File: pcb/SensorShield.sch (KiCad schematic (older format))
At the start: 58 parts, among them U14 ICE40UP5K-SG48ITR, U15 GD25Q32CTIGR-Memory_Flash

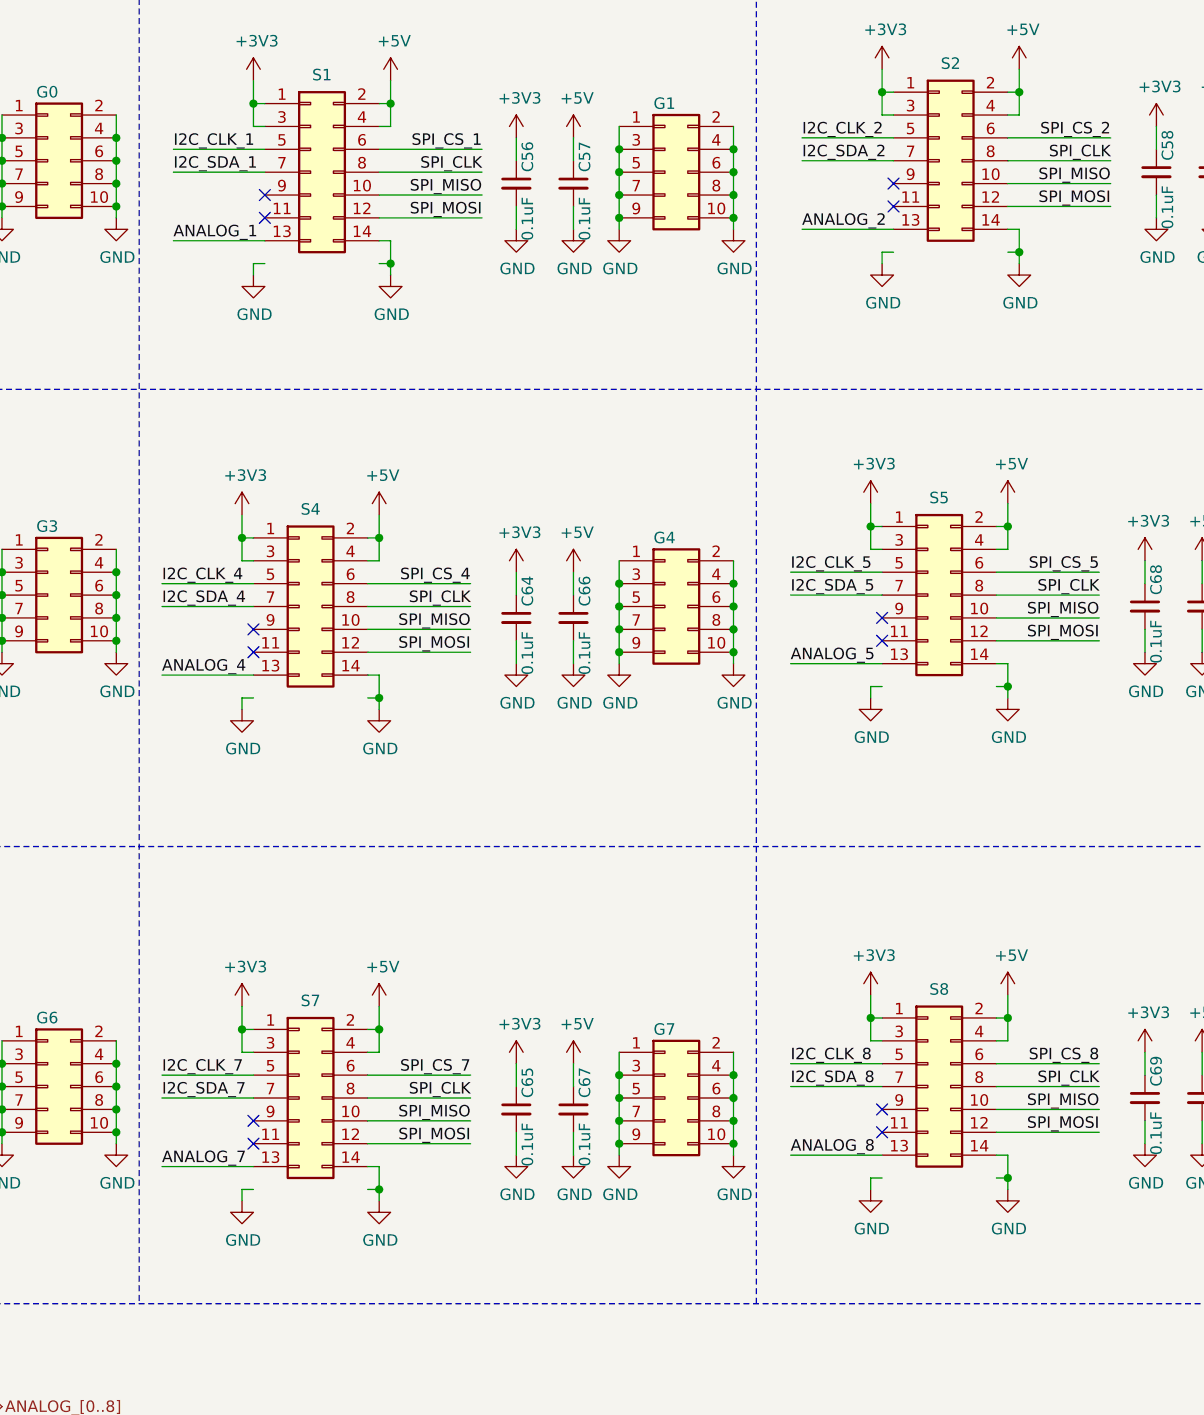
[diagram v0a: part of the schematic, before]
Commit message: routing i2c signals
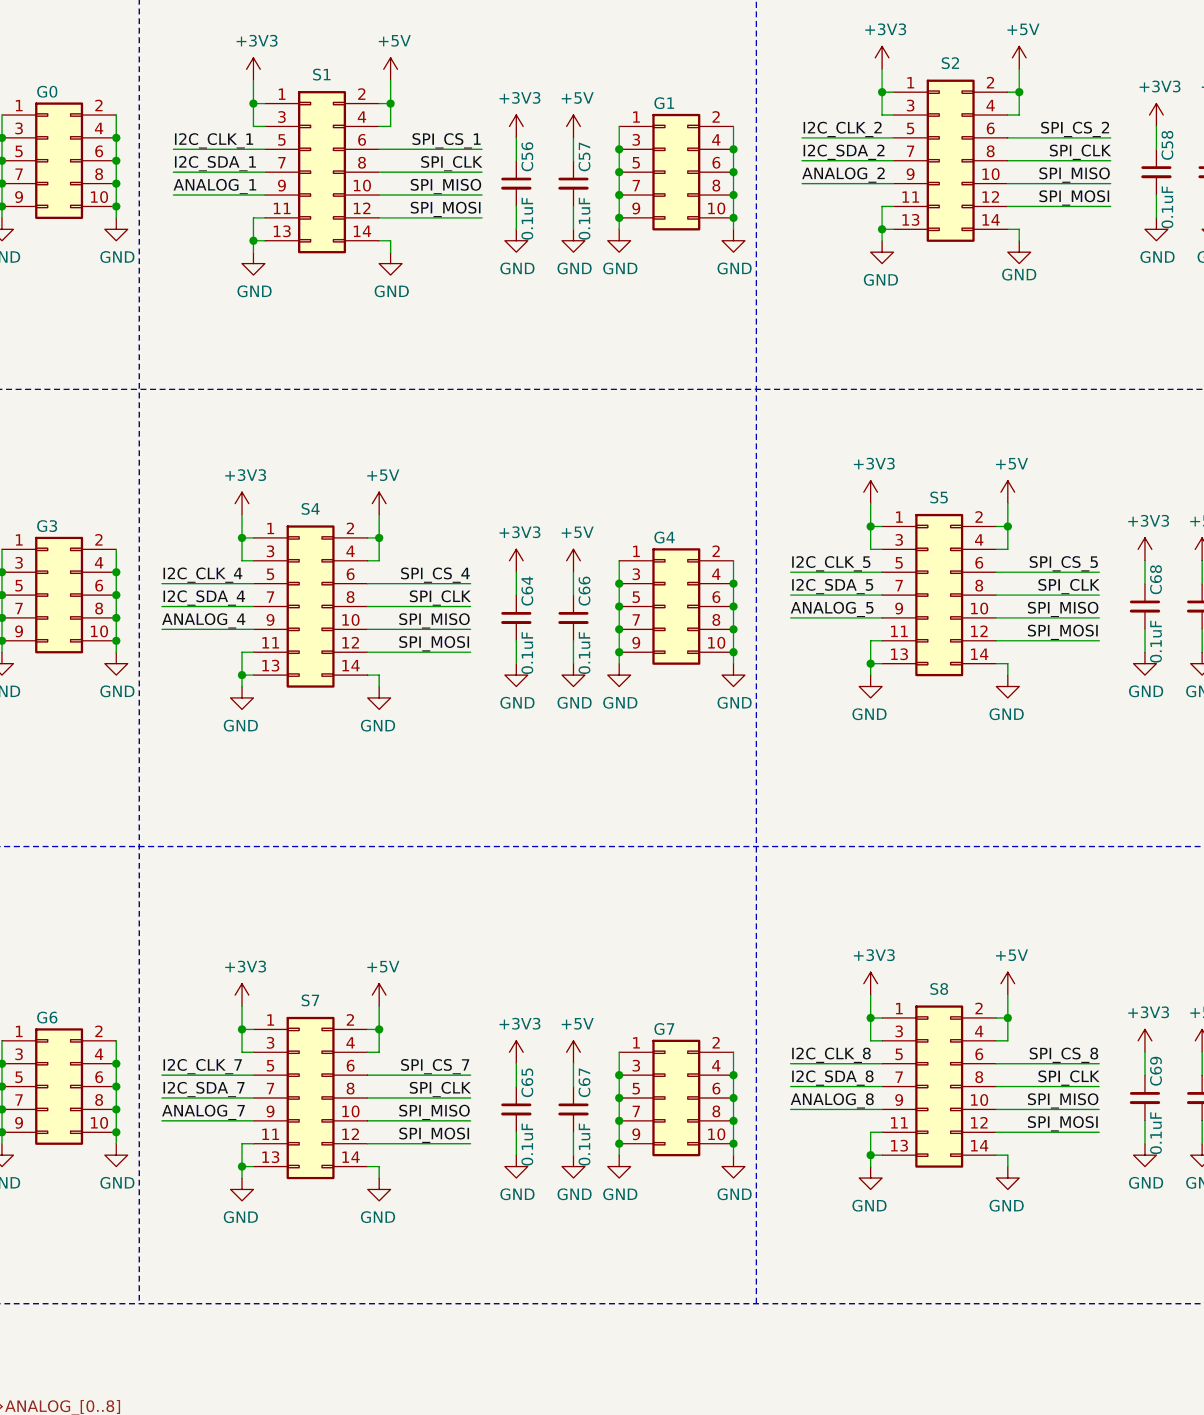
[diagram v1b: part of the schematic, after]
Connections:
- no-connect marks 12 -> 0

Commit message: 2.5V  diode placement
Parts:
- D4: value 1N4148WT-7 -> CDBU0520; symbol UPduino_v3.0:Diode_1N4148W -> Device:D
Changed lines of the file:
@@
 +1.2V_CORE
 $Comp
-L UPduino_v3.0:Diode_1N4148W D?
+L Device:D D?
 U 1 1 5E9D8B98
 P 2450 6300
@@
 AR Path="/5E9C016D/5E9D8B98" Ref="D4"  Part="1"
 F 0 "D4" H 2450 6517 50  0000 C CNN
-F 1 "1N4148WT-7" H 2450 6426 50  0000 C CNN
+F 1 "CDBU0520" H 2450 6426 50  0000 C CNN
 F 2 "Diode_SMD:D_SOD-523" H 2450 6125 50  0001 C CNN
 F 3 "https://www.vishay.com/docs/85748/1n4148w.pdf" H 2450 6300 50  0001 C CNN

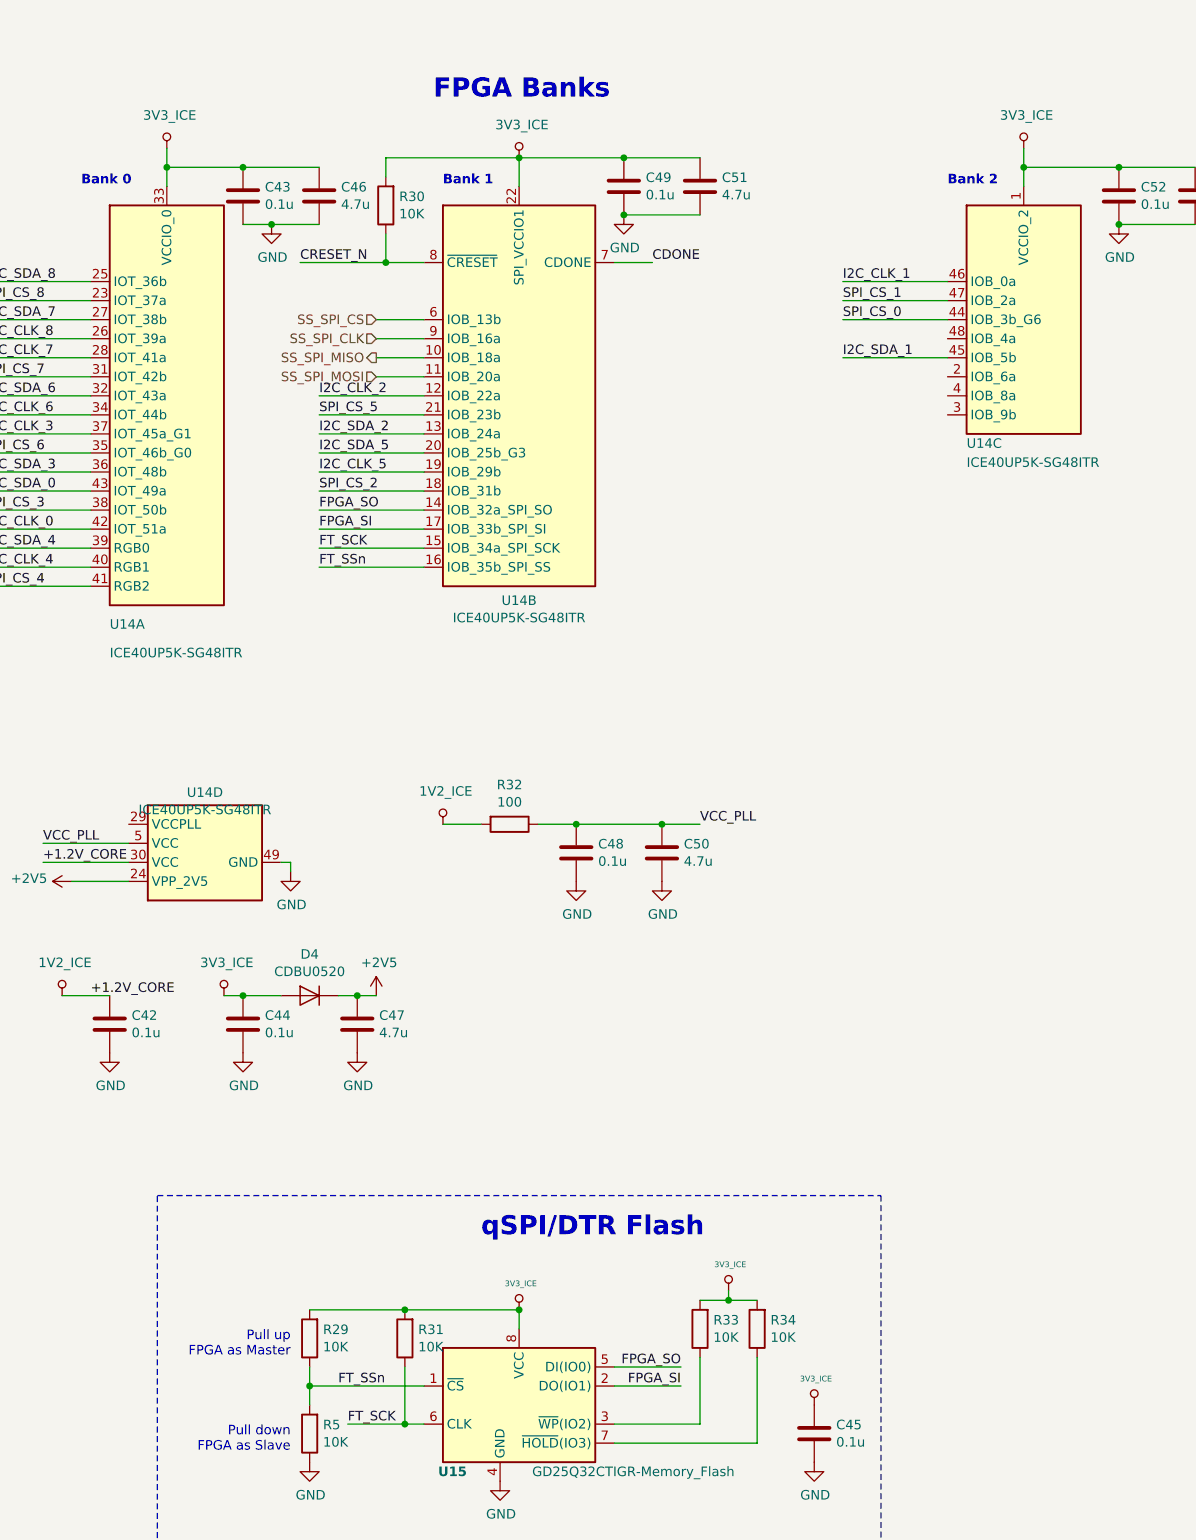
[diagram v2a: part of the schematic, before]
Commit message: 3v3_ice removed
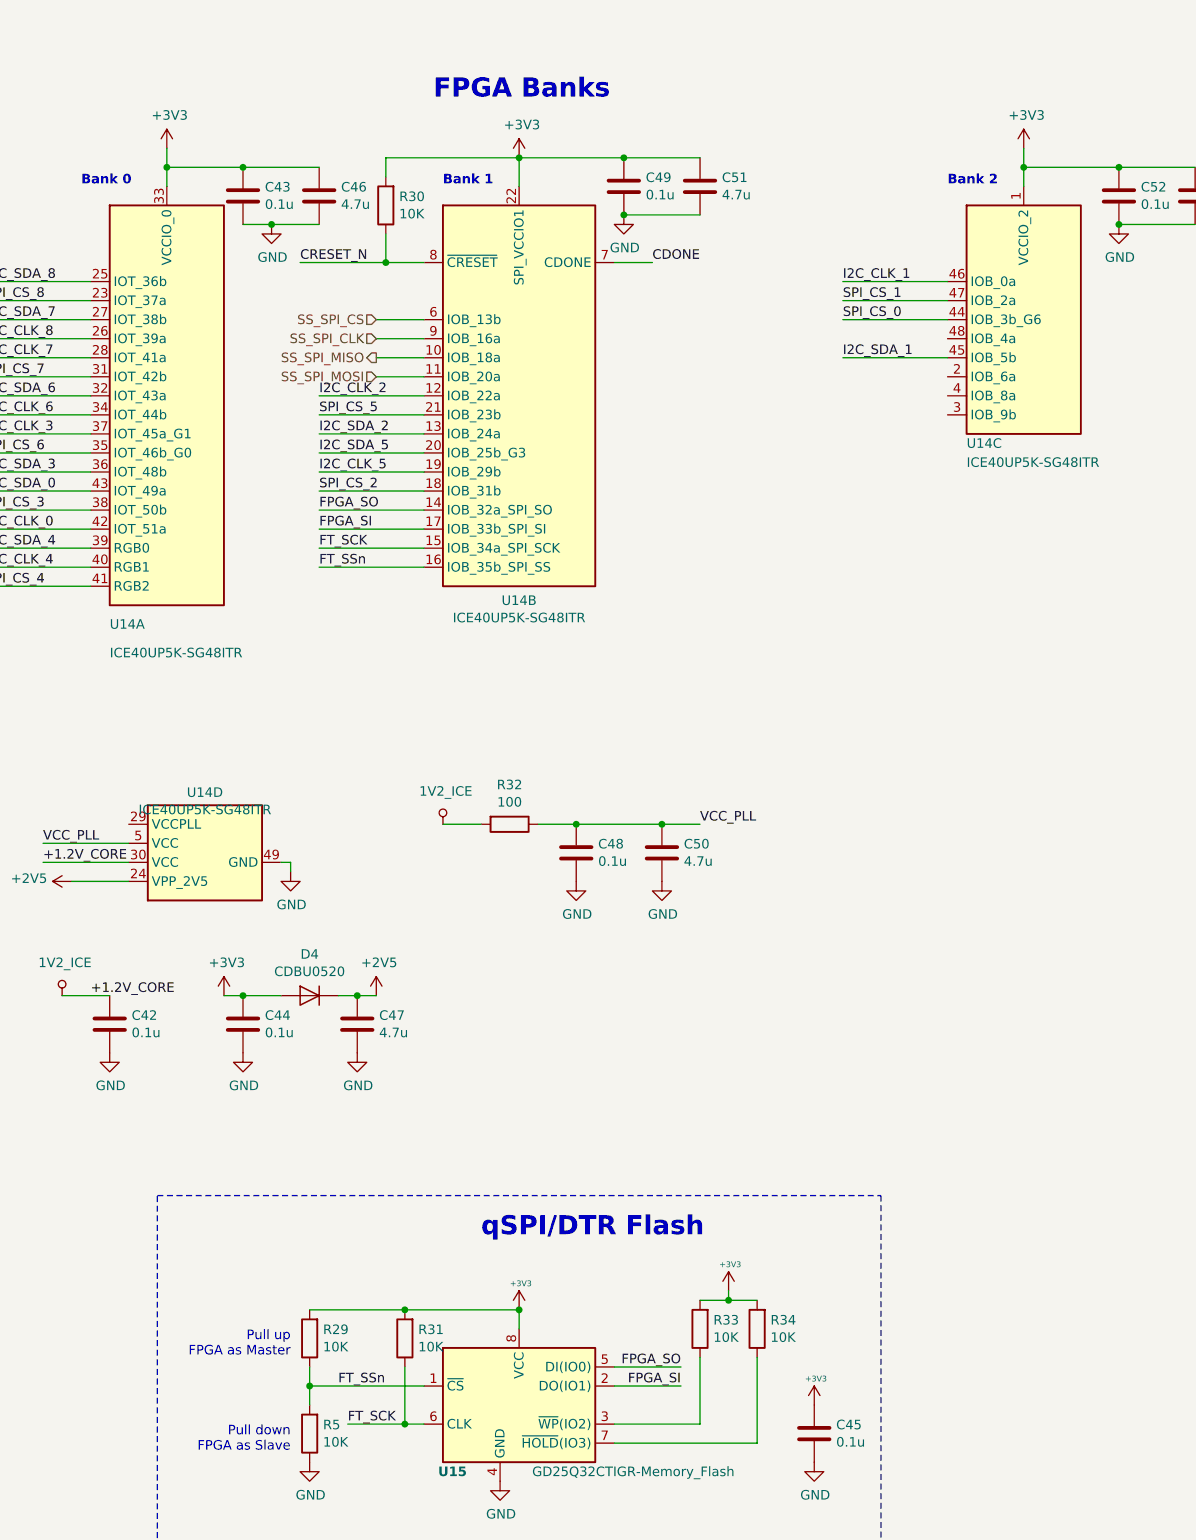
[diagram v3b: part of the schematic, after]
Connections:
- net 3V3_ICE is gone; now on net +3V3: C43.1, C44.1, C45.1, C46.1, C49.1, C51.1, C52.1, C53.1, D4.2 (A), R29.2, R30.2, R31.2, R33.2, R34.2, U14.1 (VCCIO_2), U14.22 (SPI_VCCIO1), U14.33 (VCCIO_0), U15.8 (VCC)
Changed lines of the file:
@@
 $EndComp
 $Comp
-L ventilator-PowerSymbols:3V3_ICE #PWR?
+L power:+3V3 #PWR?
 U 1 1 5E9D8A5A
 P 3550 1900
@@
 AR Path="/5E9C016D/5E9D8A5A" Ref="#PWR022"  Part="1"
 F 0 "#PWR022" H 3550 1750 50  0001 C CNN
-F 1 "3V3_ICE" H 3565 2073 50  0000 C CNN
+F 1 "+3V3" H 3565 2073 50  0000 C CNN
 F 2 "" H 3550 1900 50  0001 C CNN
 F 3 "" H 3550 1900 50  0001 C CNN
@@
 	3150 5400 3350 5400
 $Comp
-L ventilator-PowerSymbols:3V3_ICE #PWR?
+L power:+3V3 #PWR?
 U 1 1 5E9D8B03
 P 2000 6300
@@
 AR Path="/5E9C016D/5E9D8B03" Ref="#PWR05"  Part="1"
 F 0 "#PWR05" H 2000 6150 50  0001 C CNN
-F 1 "3V3_ICE" H 2015 6473 50  0000 C CNN
+F 1 "+3V3" H 2015 6473 50  0000 C CNN
 F 2 "" H 2000 6300 50  0001 C CNN
 F 3 "" H 2000 6300 50  0001 C CNN
@@
 Connection ~ 1700 1950
 $Comp
-L ventilator-PowerSymbols:3V3_ICE #PWR?
+L power:+3V3 #PWR?
 U 1 1 5E9D8BBB
 P 1700 1850
@@
 AR Path="/5E9C016D/5E9D8BBB" Ref="#PWR04"  Part="1"
 F 0 "#PWR04" H 1700 1700 50  0001 C CNN
-F 1 "3V3_ICE" H 1715 2023 50  0000 C CNN
+F 1 "+3V3" H 1715 2023 50  0000 C CNN
 F 2 "" H 1700 1850 50  0001 C CNN
 F 3 "" H 1700 1850 50  0001 C CNN
@@
 	6200 1850 6200 1950
 $Comp
-L ventilator-PowerSymbols:3V3_ICE #PWR?
+L power:+3V3 #PWR?
 U 1 1 5E9D8BCF
 P 6200 1850
@@
 AR Path="/5E9C016D/5E9D8BCF" Ref="#PWR029"  Part="1"
 F 0 "#PWR029" H 6200 1700 50  0001 C CNN
-F 1 "3V3_ICE" H 6215 2023 50  0000 C CNN
+F 1 "+3V3" H 6215 2023 50  0000 C CNN
 F 2 "" H 6200 1850 50  0001 C CNN
 F 3 "" H 6200 1850 50  0001 C CNN
@@
 $EndComp
 $Comp
-L ventilator-PowerSymbols:3V3_ICE #PWR0232
+L power:+3V3 #PWR0232
 U 1 1 5EA595EA
 P 3550 7950
 F 0 "#PWR0232" H 3550 7910 30  0001 C CNN
-F 1 "3V3_ICE" H 3559 8088 30  0000 C CNN
+F 1 "+3V3" H 3559 8088 30  0000 C CNN
 F 2 "" H 3550 7950 60  0000 C CNN
 F 3 "" H 3550 7950 60  0000 C CNN
@@
 	4500 7900 4650 7900
 $Comp
-L ventilator-PowerSymbols:3V3_ICE #PWR0233
+L power:+3V3 #PWR0233
 U 1 1 5EA5A432
 P 4650 7850
 F 0 "#PWR0233" H 4650 7810 30  0001 C CNN
-F 1 "3V3_ICE" H 4659 7988 30  0000 C CNN
+F 1 "+3V3" H 4659 7988 30  0000 C CNN
 F 2 "" H 4650 7850 60  0000 C CNN
 F 3 "" H 4650 7850 60  0000 C CNN
@@
 	4800 8200 4800 8650
 $Comp
-L ventilator-PowerSymbols:3V3_ICE #PWR0235
+L power:+3V3 #PWR0235
 U 1 1 5EB76CE1
 P 5100 8450
 F 0 "#PWR0235" H 5100 8410 30  0001 C CNN
-F 1 "3V3_ICE" H 5109 8588 30  0000 C CNN
+F 1 "+3V3" H 5109 8588 30  0000 C CNN
 F 2 "" H 5100 8450 60  0000 C CNN
 F 3 "" H 5100 8450 60  0000 C CNN

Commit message: footprint fix
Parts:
- C42, C44: footprint Resistor_SMD:R_0402_1005Metric -> Capacitor_SMD:C_0402_1005Metric
- C47: footprint Resistor_SMD:R_0402_1005Metric -> Capacitor_SMD:C_0603_1608Metric
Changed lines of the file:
@@
 F 0 "C44" H 2215 6496 50  0000 L CNN
 F 1 "0.1u" H 2215 6405 50  0000 L CNN
-F 2 "Resistor_SMD:R_0402_1005Metric" H 2138 6300 50  0001 C CNN
+F 2 "Capacitor_SMD:C_0402_1005Metric" H 2138 6300 50  0001 C CNN
 F 3 "~" H 2100 6450 50  0001 C CNN
 	1    2100 6450
@@
 F 0 "C42" H 1515 6496 50  0000 L CNN
 F 1 "0.1u" H 1515 6405 50  0000 L CNN
-F 2 "Resistor_SMD:R_0402_1005Metric" H 1438 6300 50  0001 C CNN
+F 2 "Capacitor_SMD:C_0402_1005Metric" H 1438 6300 50  0001 C CNN
 F 3 "~" H 1400 6450 50  0001 C CNN
 	1    1400 6450
@@
 F 0 "C47" H 2815 6496 50  0000 L CNN
 F 1 "4.7u" H 2815 6405 50  0000 L CNN
-F 2 "Resistor_SMD:R_0402_1005Metric" H 2738 6300 50  0001 C CNN
+F 2 "Capacitor_SMD:C_0603_1608Metric" H 2738 6300 50  0001 C CNN
 F 3 "~" H 2700 6450 50  0001 C CNN
 	1    2700 6450
@@
 	-1   0    0    -1
 $EndComp
-Wire Bus Line
-	2250 9700 2250 10200
-Wire Bus Line
-	9700 7600 9700 8450
 Text Label 750  2550 0    50   ~ 0
 I2C_SDA_8
 Text Label 750  2850 0    50   ~ 0
 I2C_CLK_8
+Wire Bus Line
+	2250 9700 2250 10200
+Wire Bus Line
+	9700 7600 9700 8450
 $EndSCHEMATC
